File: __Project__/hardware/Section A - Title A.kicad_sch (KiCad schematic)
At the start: 0 parts

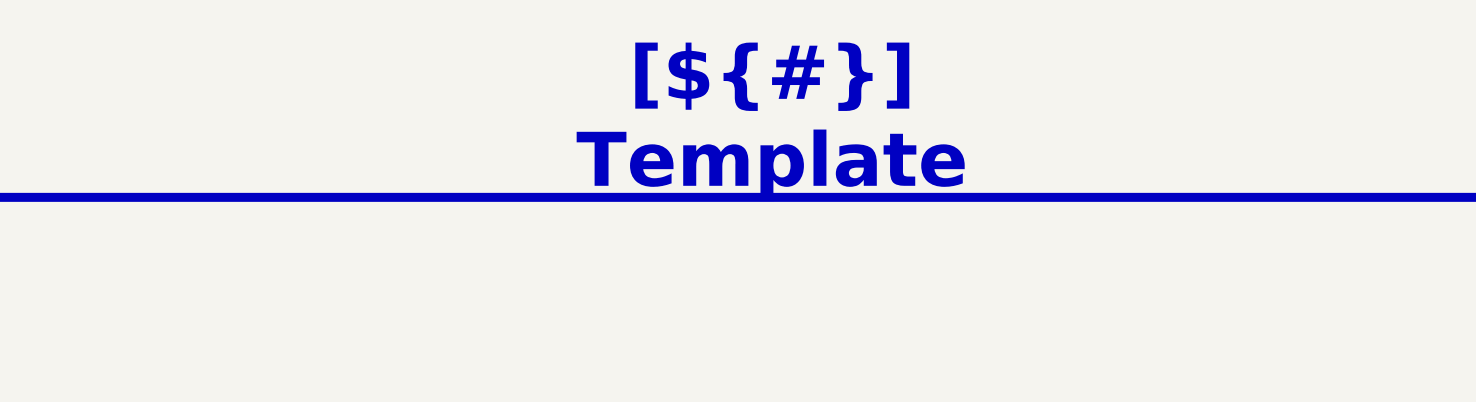
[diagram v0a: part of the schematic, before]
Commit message: Fix JST footprints
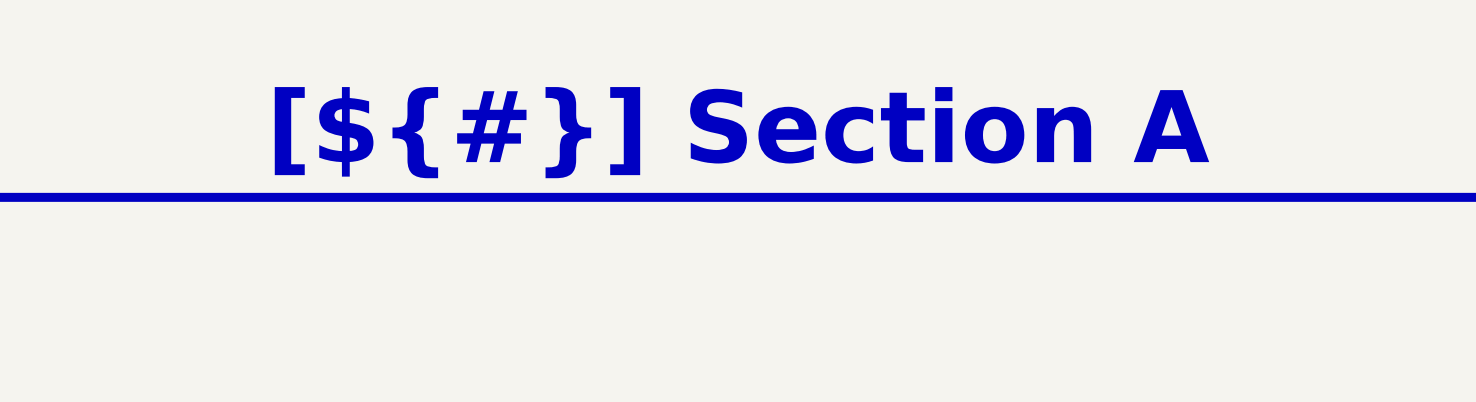
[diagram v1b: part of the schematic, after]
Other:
- title: Template -> Section A
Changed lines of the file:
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@@
 	(paper "A4")
 	(title_block
-		(title "Template")
+		(title "Section A")
 		(date "2025-06-05")
 		(rev "${REVISION}")
@@
 	(text_box "[${#}] ${TITLE}"
 		(exclude_from_sim no)
-		(at 115.57 15.24 0)
-		(size 72.39 12.7)
-		(margins 4.4999 4.4999 4.4999 4.4999)
+		(at 12.7 12.7 0)
+		(size 270.51 20.32)
+		(margins 5.9999 5.9999 5.9999 5.9999)
 		(stroke
 			(width -0.0001)
@@
 			(font
 				(face "Times New Roman")
-				(size 6 6)
+				(size 8 8)
 				(thickness 1.2)
 				(bold yes)
